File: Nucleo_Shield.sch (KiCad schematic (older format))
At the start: 4 parts, among them CN5 Digital, CN6 Power, CN8 Analog, CN9 Digital

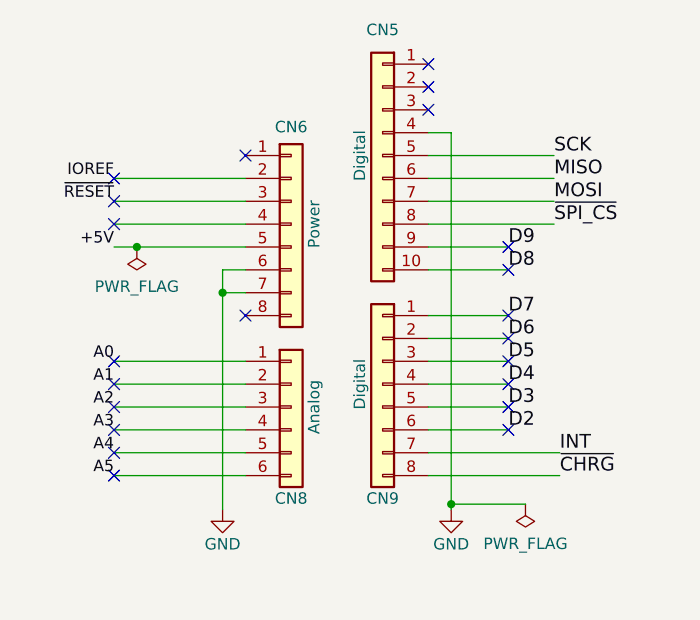
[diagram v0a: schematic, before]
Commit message: Clean up and make template project
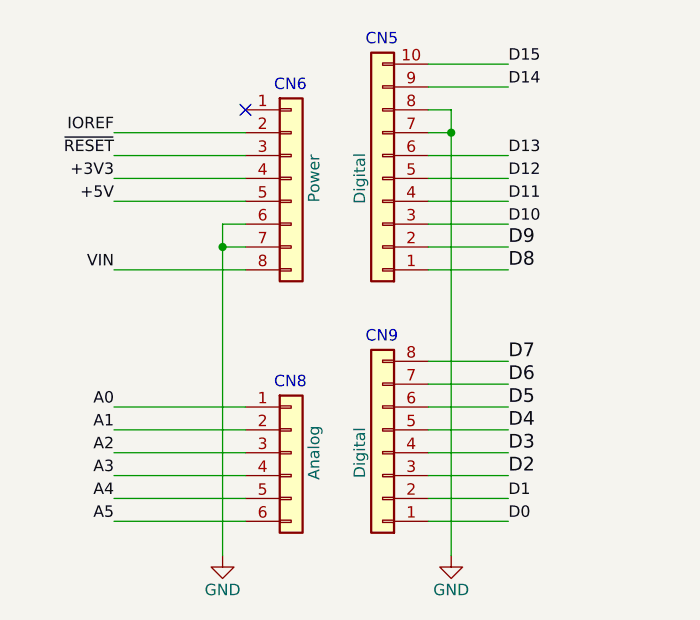
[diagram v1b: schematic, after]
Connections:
- net INT is gone; now on net D6: CN9.7 (Pin_7)
- net MOSI is gone; now on net GND: CN5.7 (Pin_7)
- net ~CHRG is gone; now on net D7: CN9.8 (Pin_8)
- net ~SPI_CS is gone; now on net GND: CN5.8 (Pin_8)
- net D2: now also CN9.3 (Pin_3); no longer CN9.6 (Pin_6)
- net D3: now also CN9.4 (Pin_4); no longer CN9.5 (Pin_5)
- net D4: now also CN9.5 (Pin_5); no longer CN9.4 (Pin_4)
- net D5: now also CN9.6 (Pin_6); no longer CN9.3 (Pin_3)
- net D6: no longer CN9.2 (Pin_2)
- net D7: no longer CN9.1 (Pin_1)
- net D8: now also CN5.1 (Pin_1); no longer CN5.10 (Pin_10)
- net D9: now also CN5.2 (Pin_2); no longer CN5.9 (Pin_9)
- net GND: no longer CN5.4 (Pin_4)
- net +3V3: now reaches CN6.4 (Pin_4)
- net VIN: now reaches CN6.8 (Pin_8)
- net D10: now reaches CN5.3 (Pin_3)
- net MISO renamed D13
- net SCK renamed D12
- new net D0: CN9.1 (Pin_1)
- new net D1: CN9.2 (Pin_2)
- new net D11: CN5.4 (Pin_4)
- new net D14: CN5.9 (Pin_9)
- new net D15: CN5.10 (Pin_10)
- no-connect marks 22 -> 1
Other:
- note added: "CN5"
- note added: "CN6"
- note added: "CN8"
- note added: "CN9"
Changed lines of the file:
@@
 encoding utf-8
 Sheet 1 1
-Title "Vert2 Power Schema"
-Date "2021-11-11"
+Title "Nucleo-64 Arduino Uno V3 Shield"
+Date "2021-11-13"
 Rev "1.0"
 Comp "Sid Price Software Design"
@@
 Comment4 ""
 $EndDescr
-Text Label 6625 4725 0    60   ~ 0
-~CHRG
+Text Label 6400 4725 0    60   ~ 0
+D2
+Text Label 6400 4625 0    60   ~ 0
+D3
 Text Label 6400 4525 0    60   ~ 0
-D2
-Text Label 6625 4625 0    60   ~ 0
-INT
+D4
 Text Label 6400 4425 0    60   ~ 0
-D3
+D5
 Text Label 6400 4325 0    60   ~ 0
-D4
+D6
 Text Label 6400 4225 0    60   ~ 0
-D5
-Text Label 6400 4125 0    60   ~ 0
-D6
-Text Label 6400 4025 0    60   ~ 0
 D7
 Text Label 6400 3825 0    60   ~ 0
@@
 Text Label 6400 3725 0    60   ~ 0
 D9
-Text Label 6600 3625 0    60   ~ 0
-~SPI_CS
-Text Label 6600 3525 0    60   ~ 0
-MOSI
-Text Label 6600 3425 0    60   ~ 0
-MISO
-Text Label 6600 3325 0    60   ~ 0
-SCK
 $Comp
 L Connector_Generic:Conn_01x08 CN6
 U 1 1 56D70129
-P 5450 3625
-F 0 "CN6" H 5450 4050 50  0000 C CNN
-F 1 "Power" V 5550 3625 50  0000 C CNN
-F 2 "Socket_Arduino_Uno:Socket_Strip_Arduino_1x08" V 5600 3625 20  0001 C CNN
-F 3 "" H 5450 3625 50  0000 C CNN
-	1    5450 3625
+P 5450 3425
+F 0 "CN6" H 5450 3850 50  0001 C CNN
+F 1 "Power" V 5550 3425 50  0000 C CNN
+F 2 "Socket_Arduino_Uno:Socket_Strip_Arduino_1x08" V 5600 3425 20  0001 C CNN
+F 3 "" H 5450 3425 50  0000 C CNN
+	1    5450 3425
 	1    0    0    -1
 $EndComp
@@
 L power:GND #PWR01
 U 1 1 56D70CC2
-P 5150 4875
-F 0 "#PWR01" H 5150 4625 50  0001 C CNN
-F 1 "GND" H 5150 4725 50  0000 C CNN
-F 2 "" H 5150 4875 50  0000 C CNN
-F 3 "" H 5150 4875 50  0000 C CNN
-	1    5150 4875
+P 5150 5075
+F 0 "#PWR01" H 5150 4825 50  0001 C CNN
+F 1 "GND" H 5150 4925 50  0000 C CNN
+F 2 "" H 5150 5075 50  0000 C CNN
+F 3 "" H 5150 5075 50  0000 C CNN
+	1    5150 5075
 	1    0    0    -1
 $EndComp
@@
 L power:GND #PWR02
 U 1 1 56D70CFF
-P 6150 4875
-F 0 "#PWR02" H 6150 4625 50  0001 C CNN
-F 1 "GND" H 6150 4725 50  0000 C CNN
-F 2 "" H 6150 4875 50  0000 C CNN
-F 3 "" H 6150 4875 50  0000 C CNN
-	1    6150 4875
+P 6150 5075
+F 0 "#PWR02" H 6150 4825 50  0001 C CNN
+F 1 "GND" H 6150 4925 50  0000 C CNN
+F 2 "" H 6150 5075 50  0000 C CNN
+F 3 "" H 6150 5075 50  0000 C CNN
+	1    6150 5075
 	1    0    0    -1
 $EndComp
@@
 L Connector_Generic:Conn_01x06 CN8
 U 1 1 56D70DD8
-P 5450 4425
-F 0 "CN8" H 5450 4025 50  0000 C CNN
-F 1 "Analog" V 5550 4425 50  0000 C CNN
-F 2 "Socket_Arduino_Uno:Socket_Strip_Arduino_1x06" V 5600 4475 20  0001 C CNN
-F 3 "" H 5450 4425 50  0000 C CNN
-	1    5450 4425
+P 5450 4625
+F 0 "CN8" H 5450 4225 50  0001 C CNN
+F 1 "Analog" V 5550 4625 50  0000 C CNN
+F 2 "Socket_Arduino_Uno:Socket_Strip_Arduino_1x06" V 5600 4675 20  0001 C CNN
+F 3 "" H 5450 4625 50  0000 C CNN
+	1    5450 4625
 	1    0    0    -1
 $EndComp
@@
 L Connector_Generic:Conn_01x08 CN9
 U 1 1 56D7164F
-P 5850 4325
-F 0 "CN9" H 5850 3825 50  0000 C CNN
-F 1 "Digital" V 5950 4325 50  0000 C CNN
-F 2 "Socket_Arduino_Uno:Socket_Strip_Arduino_1x08" V 6000 4275 20  0001 C CNN
-F 3 "" H 5850 4325 50  0000 C CNN
-	1    5850 4325
-	-1   0    0    -1
-$EndComp
-Wire Wire Line
-	5250 3825 5150 3825
-Wire Wire Line
-	5250 3925 5150 3925
-Connection ~ 5150 3925
+P 5850 4625
+F 0 "CN9" H 5850 4125 50  0001 C CNN
+F 1 "Digital" V 5950 4625 50  0000 C CNN
+F 2 "Socket_Arduino_Uno:Socket_Strip_Arduino_1x08" V 6000 4575 20  0001 C CNN
+F 3 "" H 5850 4625 50  0000 C CNN
+	1    5850 4625
+	-1   0    0    1
+$EndComp
+Wire Wire Line
+	5250 3625 5150 3625
+Wire Wire Line
+	5250 3725 5150 3725
 $Comp
 L Connector_Generic:Conn_01x10 CN5
 U 1 1 56D721E0
-P 5850 3325
-F 0 "CN5" H 5850 3875 50  0000 C CNN
-F 1 "Digital" V 5950 3325 50  0000 C CNN
-F 2 "Socket_Arduino_Uno:Socket_Strip_Arduino_1x10" V 6000 3325 20  0001 C CNN
-F 3 "" H 5850 3325 50  0000 C CNN
-	1    5850 3325
-	-1   0    0    -1
-$EndComp
-Wire Wire Line
-	6050 4025 6400 4025
-Wire Wire Line
-	6050 4125 6400 4125
+P 5850 3425
+F 0 "CN5" H 5850 3975 50  0001 C CNN
+F 1 "Digital" V 5950 3425 50  0000 C CNN
+F 2 "Socket_Arduino_Uno:Socket_Strip_Arduino_1x10" V 6000 3425 20  0001 C CNN
+F 3 "" H 5850 3425 50  0000 C CNN
+	1    5850 3425
+	-1   0    0    1
+$EndComp
 Wire Wire Line
 	6050 4225 6400 4225
@@
 	6050 4525 6400 4525
 Wire Wire Line
-	6050 4625 6625 4625
-Wire Wire Line
-	6050 4725 6625 4725
-Wire Wire Line
-	5150 3825 5150 3925
-Wire Wire Line
-	5150 3925 5150 4875
-NoConn ~ 6400 4125
-NoConn ~ 6400 4225
-NoConn ~ 6400 4325
-NoConn ~ 6400 4425
-NoConn ~ 6400 4525
-NoConn ~ 6400 3725
-Wire Wire Line
-	5250 4225 4675 4225
-Wire Wire Line
-	5250 4325 4675 4325
+	6050 4625 6400 4625
+Wire Wire Line
+	6050 4725 6400 4725
+Wire Wire Line
+	6050 4825 6400 4825
+Wire Wire Line
+	6050 4925 6400 4925
+Wire Wire Line
+	5150 3625 5150 3725
+Wire Wire Line
+	5150 3725 5150 5075
 Wire Wire Line
 	5250 4425 4675 4425
@@
 Wire Wire Line
 	5250 4725 4675 4725
-NoConn ~ 4675 4325
-NoConn ~ 4675 4425
-NoConn ~ 4675 4525
-NoConn ~ 4675 4625
-NoConn ~ 4675 4725
-Text Label 4675 4225 2    50   ~ 0
+Wire Wire Line
+	5250 4825 4675 4825
+Wire Wire Line
+	5250 4925 4675 4925
+Text Label 4675 4425 2    50   ~ 0
 A0
-Text Label 4675 4325 2    50   ~ 0
+Text Label 4675 4525 2    50   ~ 0
 A1
-Text Label 4675 4425 2    50   ~ 0
+Text Label 4675 4625 2    50   ~ 0
 A2
-Text Label 4675 4525 2    50   ~ 0
+Text Label 4675 4725 2    50   ~ 0
 A3
-Text Label 4675 4625 2    50   ~ 0
+Text Label 4675 4825 2    50   ~ 0
 A4
-Text Label 4675 4725 2    50   ~ 0
+Text Label 4675 4925 2    50   ~ 0
 A5
-NoConn ~ 5250 3325
+NoConn ~ 5250 3125
+Wire Wire Line
+	5250 3225 4675 3225
+Wire Wire Line
+	5250 3325 4675 3325
 Wire Wire Line
 	5250 3425 4675 3425
-Wire Wire Line
-	5250 3525 4675 3525
-Wire Wire Line
-	5250 3625 4675 3625
-Wire Wire Line
-	4675 3725 4775 3725
-NoConn ~ 5250 4025
-NoConn ~ 4675 3425
+Text Label 4675 3225 2    50   ~ 0
+IOREF
+Text Label 4675 3325 2    50   ~ 0
+~RESET
+Text Label 4675 3525 2    50   ~ 0
++5V
+Wire Wire Line
+	6050 3325 6400 3325
+Wire Wire Line
+	6050 3525 6400 3525
+Wire Wire Line
+	6050 3625 6400 3625
+Wire Wire Line
+	6050 3725 6400 3725
+Wire Wire Line
+	6050 3825 6400 3825
+Wire Wire Line
+	6150 3225 6050 3225
+Text Notes 5375 3050 0    50   ~ 0
+CN6
+Text Notes 5775 2850 0    50   ~ 0
+CN5
+Text Notes 5375 4350 0    50   ~ 0
+CN8
+Text Notes 5775 4150 0    50   ~ 0
+CN9
+Connection ~ 5150 3725
 Text Label 4675 3425 2    50   ~ 0
-IOREF
-Text Label 4675 3525 2    50   ~ 0
-~RESET
-NoConn ~ 4675 3625
-Text Label 4675 3725 2    50   ~ 0
-+5V
-Wire Wire Line
-	6050 3325 6600 3325
-Wire Wire Line
-	6050 3425 6600 3425
-Wire Wire Line
-	6050 3525 6600 3525
-Wire Wire Line
-	6050 3625 6600 3625
-Wire Wire Line
-	6050 3725 6400 3725
-Wire Wire Line
-	6050 3825 6400 3825
-Wire Wire Line
-	6150 3225 6050 3225
-Wire Wire Line
-	6150 3225 6150 4850
-NoConn ~ 6050 3125
-NoConn ~ 6050 3025
-NoConn ~ 6050 2925
-NoConn ~ 4675 3525
-$Comp
-L power:PWR_FLAG #FLG0101
-U 1 1 6194BB7A
-P 6475 4850
-F 0 "#FLG0101" H 6475 4925 50  0001 C CNN
-F 1 "PWR_FLAG" H 6475 5023 50  0000 C CNN
-F 2 "" H 6475 4850 50  0001 C CNN
-F 3 "~" H 6475 4850 50  0001 C CNN
-	1    6475 4850
-	-1   0    0    1
-$EndComp
-Wire Wire Line
-	6475 4850 6150 4850
-Connection ~ 6150 4850
-Wire Wire Line
-	6150 4850 6150 4875
-$Comp
-L power:PWR_FLAG #FLG0102
-U 1 1 6194E618
-P 4775 3725
-F 0 "#FLG0102" H 4775 3800 50  0001 C CNN
-F 1 "PWR_FLAG" H 4775 3898 50  0000 C CNN
-F 2 "" H 4775 3725 50  0001 C CNN
-F 3 "~" H 4775 3725 50  0001 C CNN
-	1    4775 3725
-	-1   0    0    1
-$EndComp
-Connection ~ 4775 3725
-Wire Wire Line
-	4775 3725 5250 3725
-NoConn ~ 6400 3825
-NoConn ~ 4675 4225
-NoConn ~ 6400 4025
++3V3
+Wire Wire Line
+	4675 3525 5250 3525
+Wire Wire Line
+	5250 3825 4675 3825
+Text Label 4675 3825 2    50   ~ 0
+VIN
+Text Label 6400 4925 0    50   ~ 0
+D0
+Text Label 6400 4825 0    50   ~ 0
+D1
+Wire Wire Line
+	6150 3125 6050 3125
+Wire Wire Line
+	6050 3025 6400 3025
+Wire Wire Line
+	6400 2925 6050 2925
+Text Label 6400 3625 0    50   ~ 0
+D10
+Text Label 6400 3525 0    50   ~ 0
+D11
+Wire Wire Line
+	6050 3425 6400 3425
+Text Label 6400 3425 0    50   ~ 0
+D12
+Text Label 6400 3325 0    50   ~ 0
+D13
+Wire Wire Line
+	6150 3125 6150 3225
+Connection ~ 6150 3225
+Text Label 6400 3025 0    50   ~ 0
+D14
+Text Label 6400 2925 0    50   ~ 0
+D15
+Wire Wire Line
+	6150 3225 6150 5075
 $EndSCHEMATC
